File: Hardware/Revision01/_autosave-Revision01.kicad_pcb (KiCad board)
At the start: 2 copper layers, 50 parts, among them J2 Conn_02x08_Odd_Even, J3 Conn_01x04, J4 Conn_02x08_Odd_Even, Q2 PMV32UP,215, Q3 PMV32UP,215, U1 NUCLEO-L476RG, U10 NCP1117LPST50T3G, U2 MRF89XAM9AT-I/RM, U4 ICM-45605

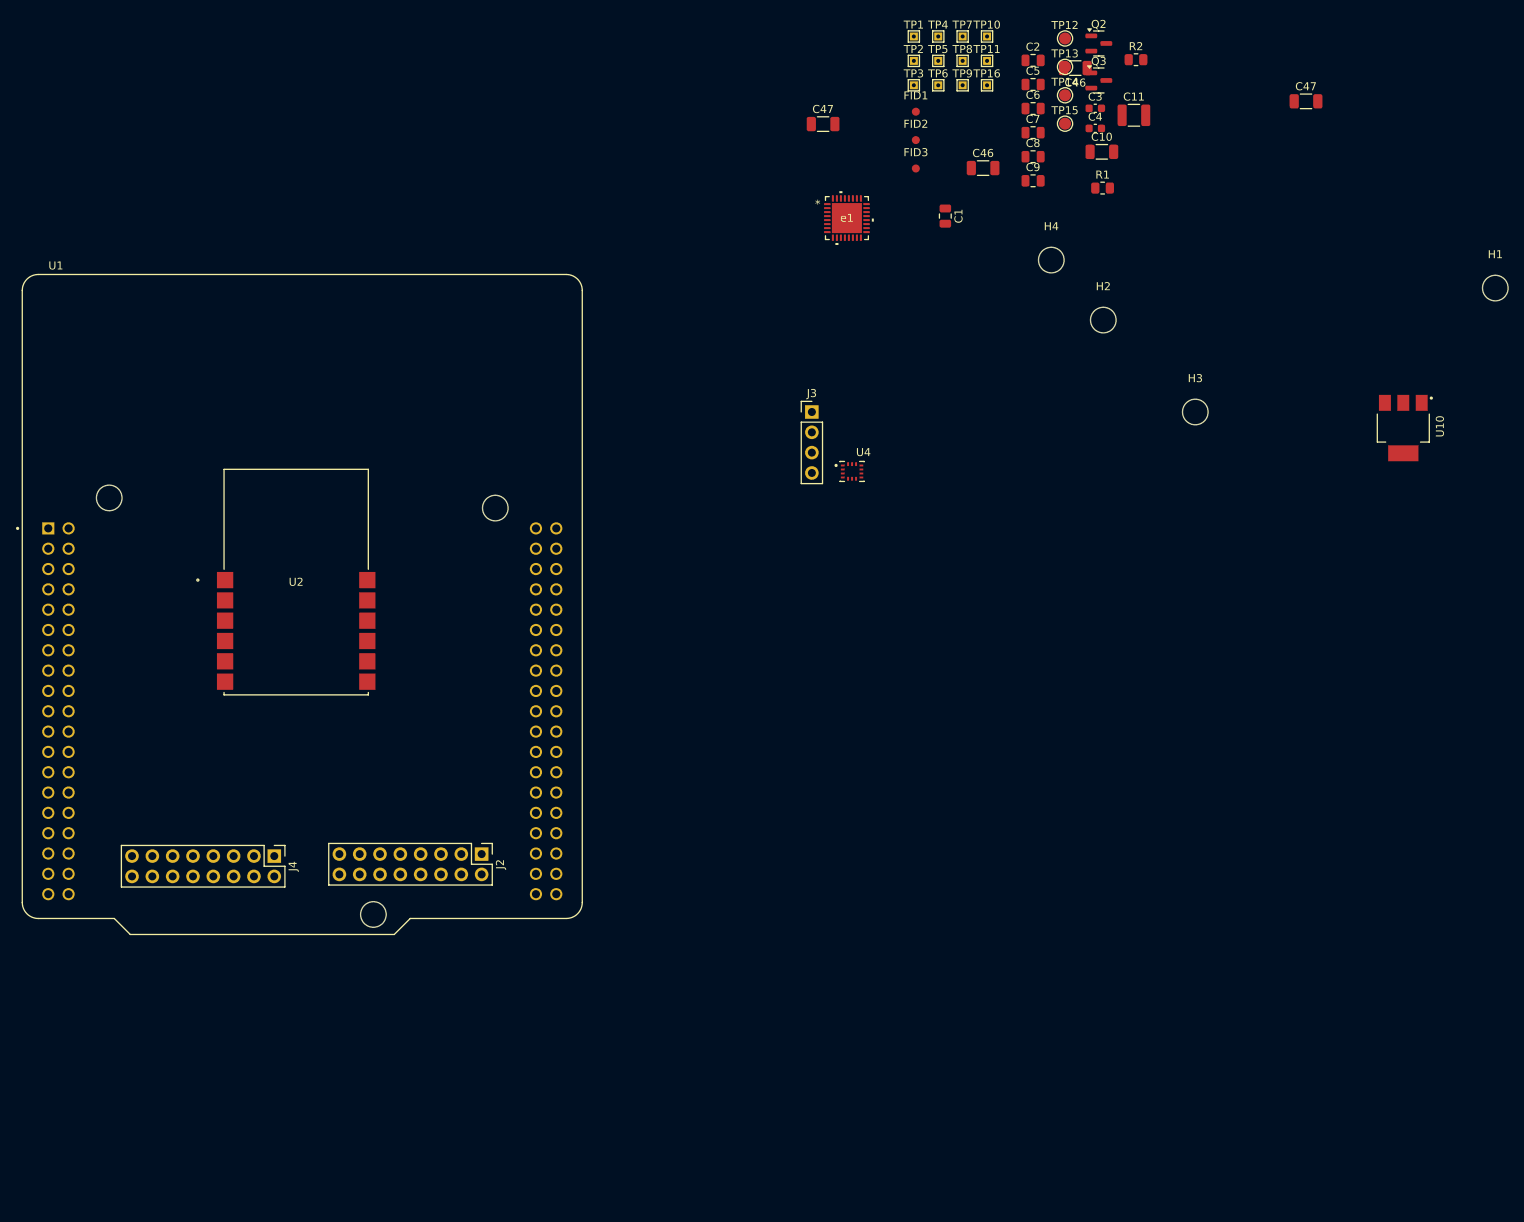
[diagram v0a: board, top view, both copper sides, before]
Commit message: ADDED 25pF to STRAIN GAUGES to remove noise ADDED FOOTPRINTS TO COMPONENTS Changed PS back to external-highside switch as internal mosfet current rating is too low pull-up for PMOS strainV_enable added Reconfigured new Nucleo board STM32IDE file
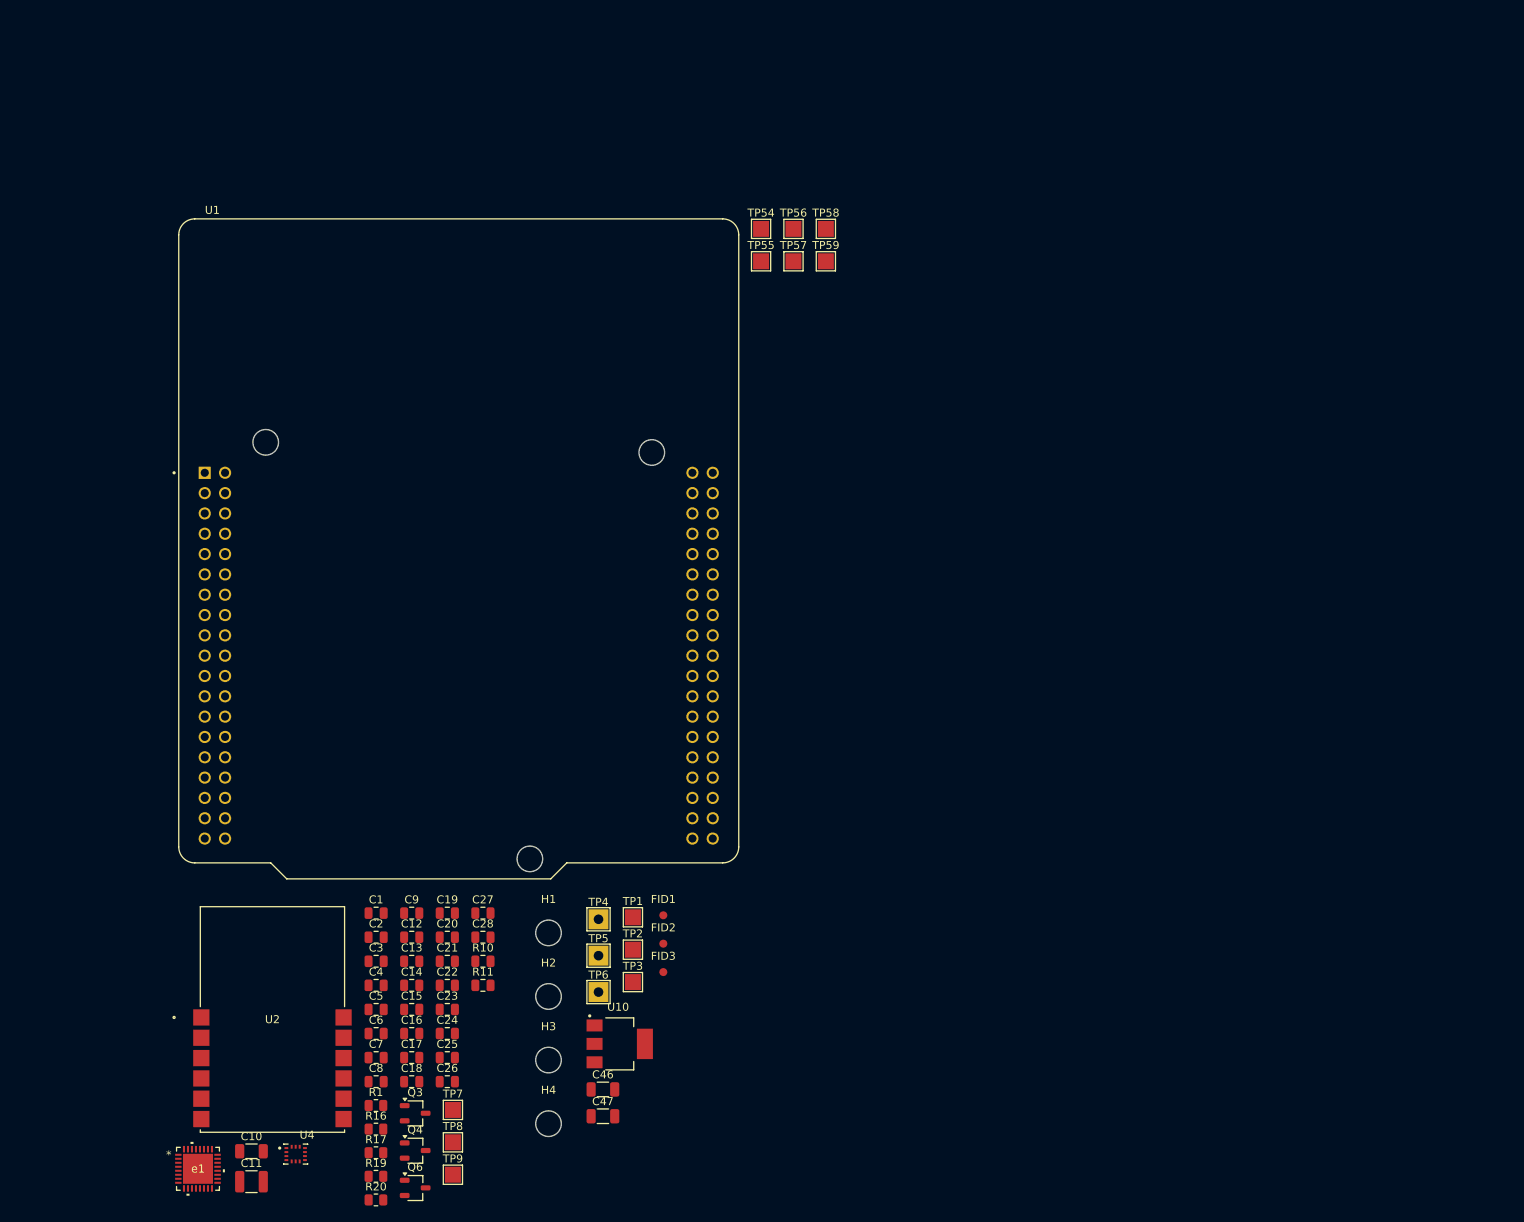
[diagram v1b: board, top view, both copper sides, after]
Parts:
- removed the C46 at (219.0, 34.5)
- removed the C46 at (207.5, 47.0)
- removed the C47 at (187.5, 41.5)
- removed the C47 at (247.8, 38.7)
- removed J2, J4: Conn_02x08_Odd_Even, Connector_PinHeader_2.54mm:PinHeader_2x08_P2.54mm_Vertical
- removed J3: Conn_01x04, Connector_PinHeader_2.54mm:PinHeader_1x04_P2.54mm_Vertical
- removed Q2: PMV32UP,215, Package_TO_SOT_SMD:SOT-23
- removed R2: 33K +-5%, Resistor_SMD:R_0805_2012Metric
- removed TP10, TP11, TP16: TestPoint, TestPoint:TestPoint_THTPad_1.0x1.0mm_Drill0.5mm
- removed TP12, TP13, TP14, TP15: VBattery_Div_Enable, TestPoint:TestPoint_Pad_D1.5mm
- added C12: 0.1uF, Capacitor_SMD:C_0805_2012Metric, F.Cu at (136.1, 143.1)
- added C13: 25pF, Capacitor_SMD:C_0805_2012Metric, F.Cu at (136.1, 146.2)
- added C14: 25pF, Capacitor_SMD:C_0805_2012Metric, F.Cu at (136.1, 149.2)
- added C15: 25pF, Capacitor_SMD:C_0805_2012Metric, F.Cu at (136.1, 152.2)
- added C16: 25pF, Capacitor_SMD:C_0805_2012Metric, F.Cu at (136.1, 155.2)
- added C17: 25pF, Capacitor_SMD:C_0805_2012Metric, F.Cu at (136.1, 158.2)
- added C18: 25pF, Capacitor_SMD:C_0805_2012Metric, F.Cu at (136.1, 161.2)
- added C19: 25pF, Capacitor_SMD:C_0805_2012Metric, F.Cu at (140.5, 140.1)
- added C20: 25pF, Capacitor_SMD:C_0805_2012Metric, F.Cu at (140.5, 143.1)
- added C21: 25pF, Capacitor_SMD:C_0805_2012Metric, F.Cu at (140.5, 146.2)
- added C22: 25pF, Capacitor_SMD:C_0805_2012Metric, F.Cu at (140.5, 149.2)
- added C23: 25pF, Capacitor_SMD:C_0805_2012Metric, F.Cu at (140.5, 152.2)
- added C24: 25pF, Capacitor_SMD:C_0805_2012Metric, F.Cu at (140.5, 155.2)
- added C25: 25pF, Capacitor_SMD:C_0805_2012Metric, F.Cu at (140.5, 158.2)
- added C26: 25pF, Capacitor_SMD:C_0805_2012Metric, F.Cu at (140.5, 161.2)
- added C27: 25pF, Capacitor_SMD:C_0805_2012Metric, F.Cu at (144.9, 140.1)
- added C28: 25pF, Capacitor_SMD:C_0805_2012Metric, F.Cu at (144.9, 143.1)
- added C46: 10uF, Capacitor_SMD:C_1206_3216Metric, F.Cu at (159.9, 162.2)
- added C47: 10uF, Capacitor_SMD:C_1206_3216Metric, F.Cu at (159.9, 165.5)
- added Q4: PMOS, Package_TO_SOT_SMD:TSOT-23, F.Cu at (136.5, 169.8)
- added Q6: PMOS, Package_TO_SOT_SMD:TSOT-23, F.Cu at (136.5, 174.5)
- added R10: 0K +-1%, Capacitor_SMD:C_0805_2012Metric, F.Cu at (144.9, 146.2)
- added R11: 0k +-1%, Capacitor_SMD:C_0805_2012Metric, F.Cu at (144.9, 149.2)
- added R16: 10K +-5%, Resistor_SMD:R_0805_2012Metric, F.Cu at (131.6, 167.1)
- added R17: 10K +-5%, Resistor_SMD:R_0805_2012Metric, F.Cu at (131.6, 170.1)
- added R19: 3.3K +-1%, Resistor_SMD:R_0805_2012Metric, F.Cu at (131.6, 173.0)
- added R20: 10K +-5%, Resistor_SMD:R_0805_2012Metric, F.Cu at (131.6, 176.0)
- added TP54: TestPoint, TestPoint:TestPoint_Pad_2.0x2.0mm, F.Cu at (179.7, 54.6)
- added TP55: TestPoint, TestPoint:TestPoint_Pad_2.0x2.0mm, F.Cu at (179.7, 58.6)
- added TP56: TestPoint, TestPoint:TestPoint_Pad_2.0x2.0mm, F.Cu at (183.8, 54.6)
- added TP57: TestPoint, TestPoint:TestPoint_Pad_2.0x2.0mm, F.Cu at (183.8, 58.6)
- added TP58: TestPoint, TestPoint:TestPoint_Pad_2.0x2.0mm, F.Cu at (187.8, 54.6)
- added TP59: TestPoint, TestPoint:TestPoint_Pad_2.0x2.0mm, F.Cu at (187.8, 58.6)
- C3, C4: value 2.2uF -> 1uF; footprint Capacitor_SMD:C_0603_1608Metric -> Capacitor_SMD:C_0805_2012Metric
- Q3: value PMV32UP,215 -> NMOS; footprint Package_TO_SOT_SMD:SOT-23 -> Package_TO_SOT_SMD:TSOT-23
- R1: value 120K +-1% -> 15K +-1%
- TP1, TP2, TP3, TP7, TP8, TP9: footprint TestPoint:TestPoint_THTPad_1.0x1.0mm_Drill0.5mm -> TestPoint:TestPoint_Pad_2.0x2.0mm
- TP4, TP5, TP6: footprint TestPoint:TestPoint_THTPad_1.0x1.0mm_Drill0.5mm -> TestPoint:TestPoint_THTPad_2.5x2.5mm_Drill1.2mm
- moved C11 173.0 mm to (116.0, 173.7)
- moved C10 164.0 mm to (116.0, 169.9)
- moved Q3 154.8 mm to (136.5, 165.1)
- moved TP9 150.3 mm to (141.2, 172.8)
- moved TP8 149.4 mm to (141.2, 168.8)
- moved TP7 148.5 mm to (141.2, 164.7)
- moved R1 146.3 mm to (131.6, 164.2)
- moved e1 143.9 mm to (109.3, 172.1)
- moved H1 143.2 mm to (153.2, 142.6)
- moved C5 141.8 mm to (131.6, 152.2)
- moved C8 141.8 mm to (131.6, 161.2)
- moved C6 141.8 mm to (131.6, 155.2)
- moved C7 141.8 mm to (131.6, 158.2)
- moved C4 139.8 mm to (131.6, 149.2)
- moved C3 139.5 mm to (131.6, 146.2)
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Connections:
- Q3 pad 1: /PA1_GPIO -> Net-(Q3-D)
- Q3 pad 2: BatteryV -> /PA1_GPIO
- Q3 pad 3: Net-(Q3-D) -> GND
- R1 pad 2: Net-(Q3-D) -> Net-(Q4-D)
- TP7 pad 1: /Controller/BOOT0 -> /PC0_ADC12_IN10
- TP8 pad 1: /Controller/PA3/USART2_RX/ADC12_IN3/TIM2_CH4 -> +V_batt
- TP9 pad 1: /Controller/PA2/USART2_TX/ADC12_IN2/TIM2_CH3 -> /Application/StrainV
- U10 pad 3: BatteryV -> +V_batt
- e1 pad 12: Net-(J3-Pin_4) -> /Application/StrainV
- e1 pad 13: Net-(J3-Pin_3) -> GND
- e1 pad 25: GND -> Net-(J4-Pin_3)

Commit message: starting to work on LAYOUT
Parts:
- moved U2 101.7 mm to (143.1, 54.8)
- moved H2 77.8 mm to (117.8, 81.2)
- moved H3 77.1 mm to (166.0, 82.5)
- moved H1 9.59 mm to (151.0, 133.2)
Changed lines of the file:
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@@
 	(footprint "MountingHole:MountingHole_3.2mm_M3"
 		(layer "F.Cu")
-		(at 153.15 150.55)
+		(at 117.75 81.25)
 		(descr "Mounting Hole 3.2mm, no annular, M3")
 		(tags "mounting hole 3.2mm no annular m3")
@@
 	(footprint "MRF89XAM9AT-antenna:MOD_MRF89XAM9A_MCH"
 		(layer "F.Cu")
-		(at 118.6418 153.4252)
+		(at 143.14 54.754)
 		(tags "MRF89XAM9AT-I/RM ")
 		(property "Reference" "U2"
@@
 	(footprint "MountingHole:MountingHole_3.2mm_M3"
 		(layer "F.Cu")
-		(at 153.15 158.5)
+		(at 166 82.5)
 		(descr "Mounting Hole 3.2mm, no annular, M3")
 		(tags "mounting hole 3.2mm no annular m3")
@@
 	(footprint "MountingHole:MountingHole_3.2mm_M3"
 		(layer "F.Cu")
-		(at 153.15 142.6)
+		(at 151 133.25)
 		(descr "Mounting Hole 3.2mm, no annular, M3")
 		(tags "mounting hole 3.2mm no annular m3")
